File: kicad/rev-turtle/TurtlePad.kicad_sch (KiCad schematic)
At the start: 15 parts, among them SW1 SW_Push, U1 ProMicro

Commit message: rev1.1 again
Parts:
- removed MX8: MX-NoLED, 0xcb:SW_Cherry_MX_PCB_1.00u, symbol MX_Alps_Hybrid:MX-NoLED
- removed OL1: SSD1306, SSD1306:128x64OLED, symbol SSD1306-128x64_OLED:SSD1306
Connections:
- net GND: now also MX3.1 (COL), MX4.1 (COL), MX7.1 (COL); no longer MX3.2 (ROW), MX4.2 (ROW), MX7.2 (ROW)
- net MX3: now also MX3.2 (ROW); no longer MX3.1 (COL)
- net MX4: now also MX4.2 (ROW); no longer MX4.1 (COL)
- net MX7: now also MX7.2 (ROW); no longer MX7.1 (COL)
- net MX8: no longer names the net of U1.13 (10/PB6)
- net SCL: no longer names the net of U1.6 (3/PD0)
- net SDA: no longer names the net of U1.5 (2/PD1)
- no-connect marks 9 -> 12
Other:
- moved on the sheet: MX1, MX2, MX3, MX4, MX5, MX6, MX7

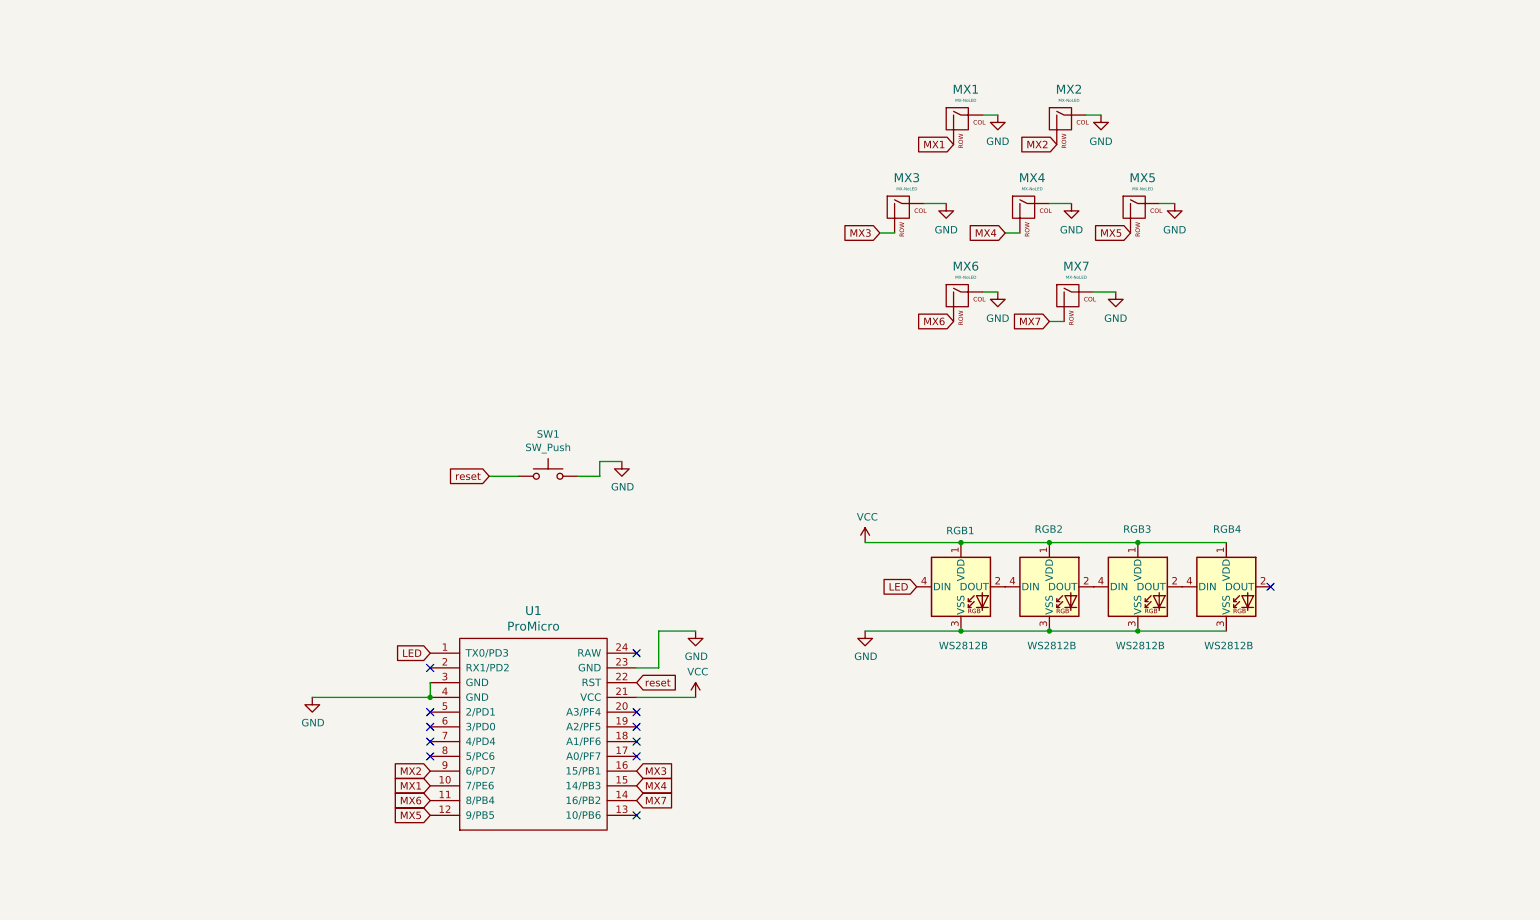
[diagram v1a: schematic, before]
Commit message: Redid schematic because I am an idiot
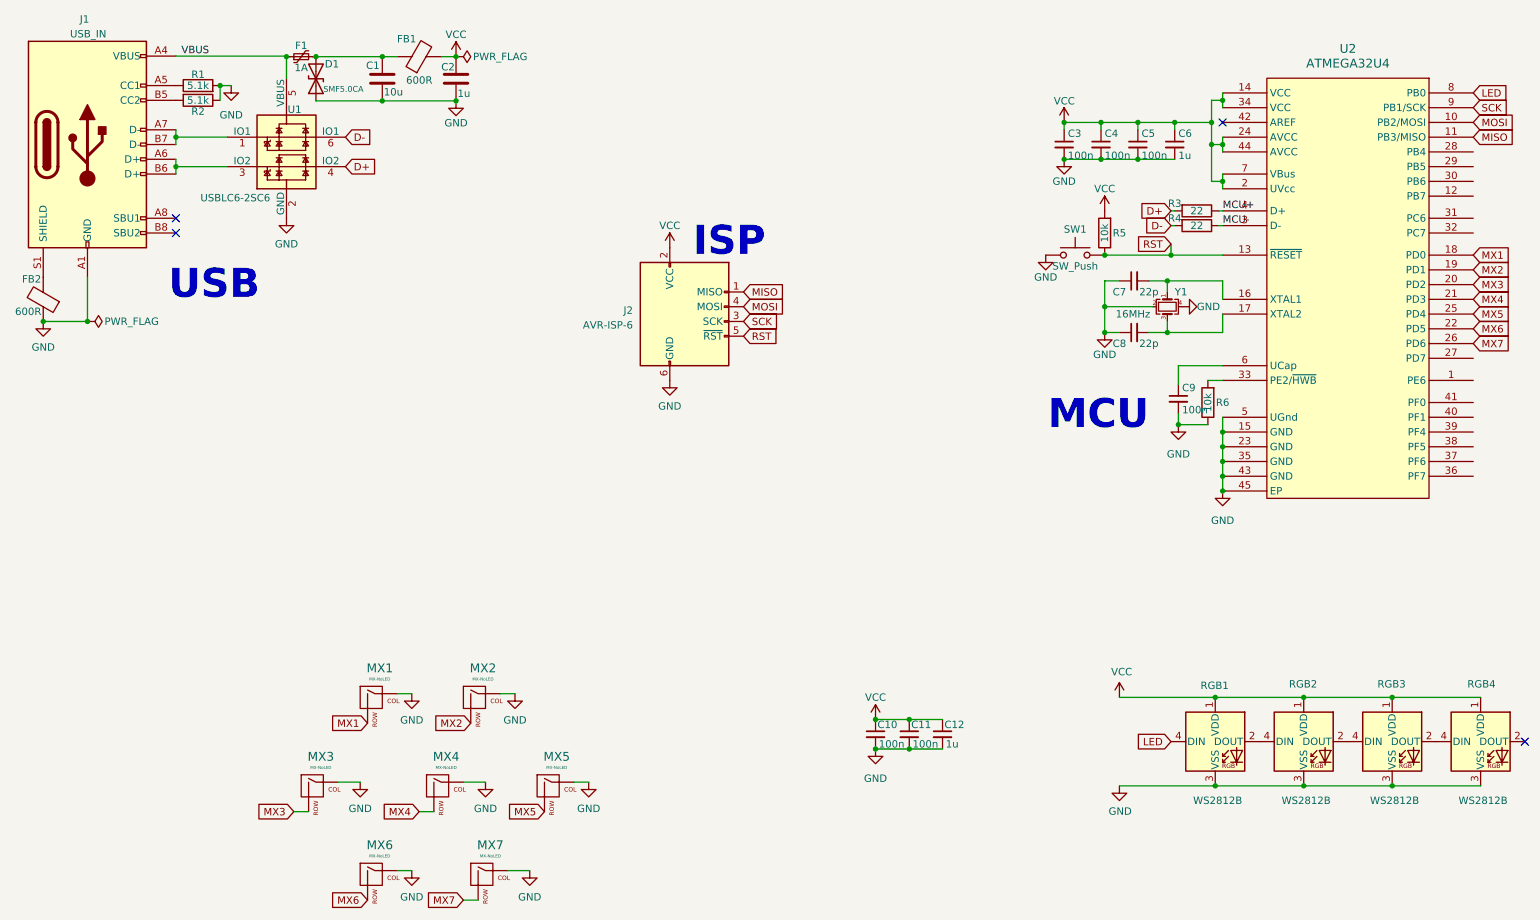
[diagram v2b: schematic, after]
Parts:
- removed U1: ProMicro, Keebio-Parts:ArduinoProMicro, symbol keebio:ProMicro
- added C1: 10u, Capacitor_SMD:C_0603_1608Metric, symbol Device:C
- added C10, C11, C3, C4, C5, C9: 100n, Capacitor_SMD:C_0603_1608Metric, symbol Device:C_Small
- added C12, C6: 1u, Capacitor_SMD:C_0603_1608Metric, symbol Device:C_Small
- added C2: 1u, Capacitor_SMD:C_0603_1608Metric, symbol Device:C
- added C7, C8: 22p, Capacitor_SMD:C_0603_1608Metric, symbol Device:C_Small
- added D1: SMF5.0CA, Diode_SMD:D_SOD-123F, symbol Device:D_TVS
- added F1: 1A, 0xcb:Fuse_0805_2012Metric, symbol Device:Polyfuse_Small
- added FB1: 600R, 0xcb:Ferrite_Bead_0603, symbol Device:FerriteBead
- added FB2: 600R, 0xcb:Ferrite_Bead_0603, symbol 0xcb:Ferrite_Bead
- added J1: USB_IN, 0xcb:molex2169900001, symbol Connector:USB_C_Receptacle_USB2.0
- added J2: AVR-ISP-6, 0xcb:AVR_PROG_2.54_THT, symbol Connector:AVR-ISP-6
- added R1, R2: 5.1k, Resistor_SMD:R_0603_1608Metric, symbol Device:R
- added R3, R4: 22, Resistor_SMD:R_0603_1608Metric, symbol Device:R
- added R5, R6: 10k, Resistor_SMD:R_0603_1608Metric, symbol Device:R
- added U1: USBLC6-2SC6, Package_TO_SOT_SMD:SOT-23-6, symbol 0xcb:USBLC6-2SC6
- added U2: ATMEGA32U4, 0xcb:QFN-44-1EP_7x7mm_P0.5mm_EP5.2x5.2mm_ThermalVias, symbol 0xcb:ATMEGA32U4
- added Y1: 16MHz, 0xcb:Crystal_SMD_3225-4Pin_3.2x2.5mm, symbol Device:Crystal_GND24_Small
- RGB1, RGB2, RGB3, RGB4: footprint Keebio-Parts:WS2812B -> LED_SMD:LED_WS2812B_PLCC4_5.0x5.0mm_P3.2mm
- SW1: footprint Keebio-Parts:SW_Tactile_SPST_Angled_MJTP1117 -> Button_Switch_SMD:SW_SPST_TL3342; Alt Part Nb. (none) -> C318884; Part Nb. (none) -> EG2531CT-ND
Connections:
- net reset is gone; now on net GND: SW1.1
- net GND: now also C1.2, C10.2, C11.2, C12.2, C2.2, C3.2, C4.2, C5.2, C6.2, C7.1, C8.1, C9.2, D1.1 (A1), FB2.1, J1.A1 (GND), J1.A12 (GND), J1.B1 (GND), J1.B12 (GND), J2.6 (GND), R1.2, R2.1, R6.1, U1.2 (GND), U2.15 (GND), U2.23 (GND), U2.35 (GND), U2.43 (GND), U2.45 (EP), U2.5 (UGnd), Y1.2, Y1.4; no longer SW1.2
- net LED: now also U2.8 (PB0)
- net MX1: now also U2.18 (PD0)
- net MX2: now also U2.19 (PD1)
- net MX3: now also U2.20 (PD2)
- net MX4: now also U2.21 (PD3)
- net MX5: now also U2.25 (PD4)
- net MX6: now also U2.22 (PD5)
- net MX7: now also U2.26 (PD6)
- net VCC: now also C10.1, C11.1, C12.1, C2.1, C3.1, C4.1, C5.1, C6.1, FB1.2, J2.2 (VCC), R5.2, U2.14 (VCC), U2.2 (UVcc), U2.24 (AVCC), U2.34 (VCC), U2.44 (AVCC), U2.7 (VBus)
- new net: J1.B5 (CC2), R2.2
- new net: FB2.2, J1.S1 (SHIELD)
- new net: C8.2, U2.17 (XTAL2), Y1.3
- new net: C7.2, U2.16 (XTAL1), Y1.1
- new net: C1.1, D1.2 (A2), F1.2, FB1.1
- new net: C9.1, U2.6 (UCap)
- new net: J1.A7 (D-), J1.B7 (D-), U1.1 (IO1)
- new net: J1.A6 (D+), J1.B6 (D+), U1.3 (IO2)
- new net: R6.2, U2.33 (PE2/~{HWB})
- new net: J1.A5 (CC1), R1.1
- new net D+: R3.2, U1.4 (IO2)
- new net D-: R4.2, U1.6 (IO1)
- new net MCU+: R3.1, U2.4 (D+)
- new net MCU-: R4.1, U2.3 (D-)
- new net MISO: J2.1 (MISO), U2.11 (PB3/MISO)
- new net MOSI: J2.4 (MOSI), U2.10 (PB2/MOSI)
- new net RST: J2.5 (~{RST}), R5.1, SW1.2, U2.13 (~{RESET})
- new net SCK: J2.3 (SCK), U2.9 (PB1/SCK)
- new net VBUS: F1.1, J1.A4 (VBUS), J1.A9 (VBUS), J1.B4 (VBUS), J1.B9 (VBUS), U1.5 (VBUS)
- no-connect marks 12 -> 4
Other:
- note added: "ISP"
- note added: "MCU"
- note added: "USB"
- moved on the sheet: MX1, MX2, MX3, MX4, MX5, MX6, MX7, RGB1, RGB2, RGB3, RGB4

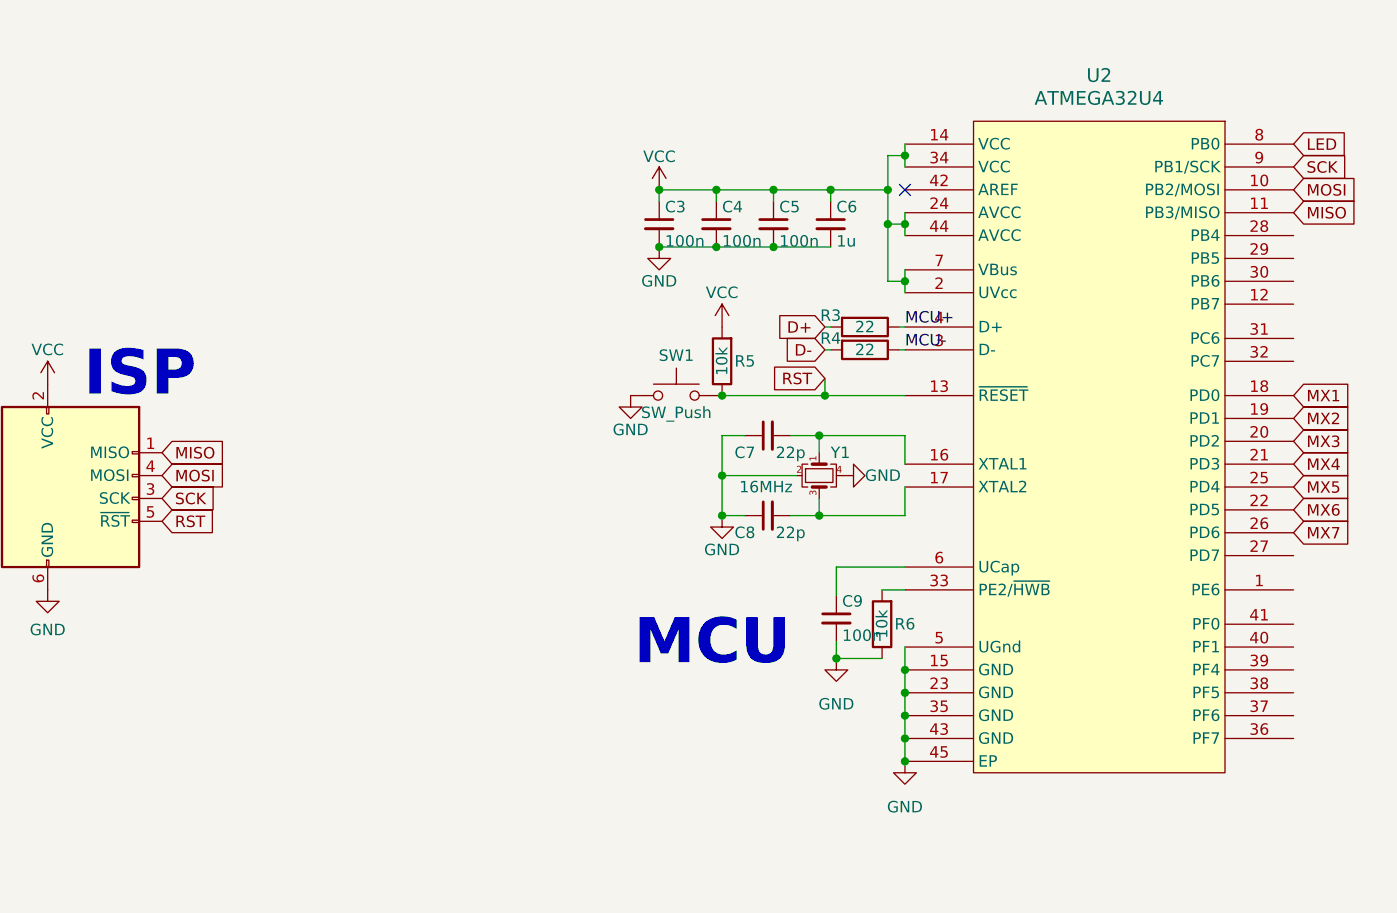
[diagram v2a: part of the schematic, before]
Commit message: Placed and routed all components on PCB
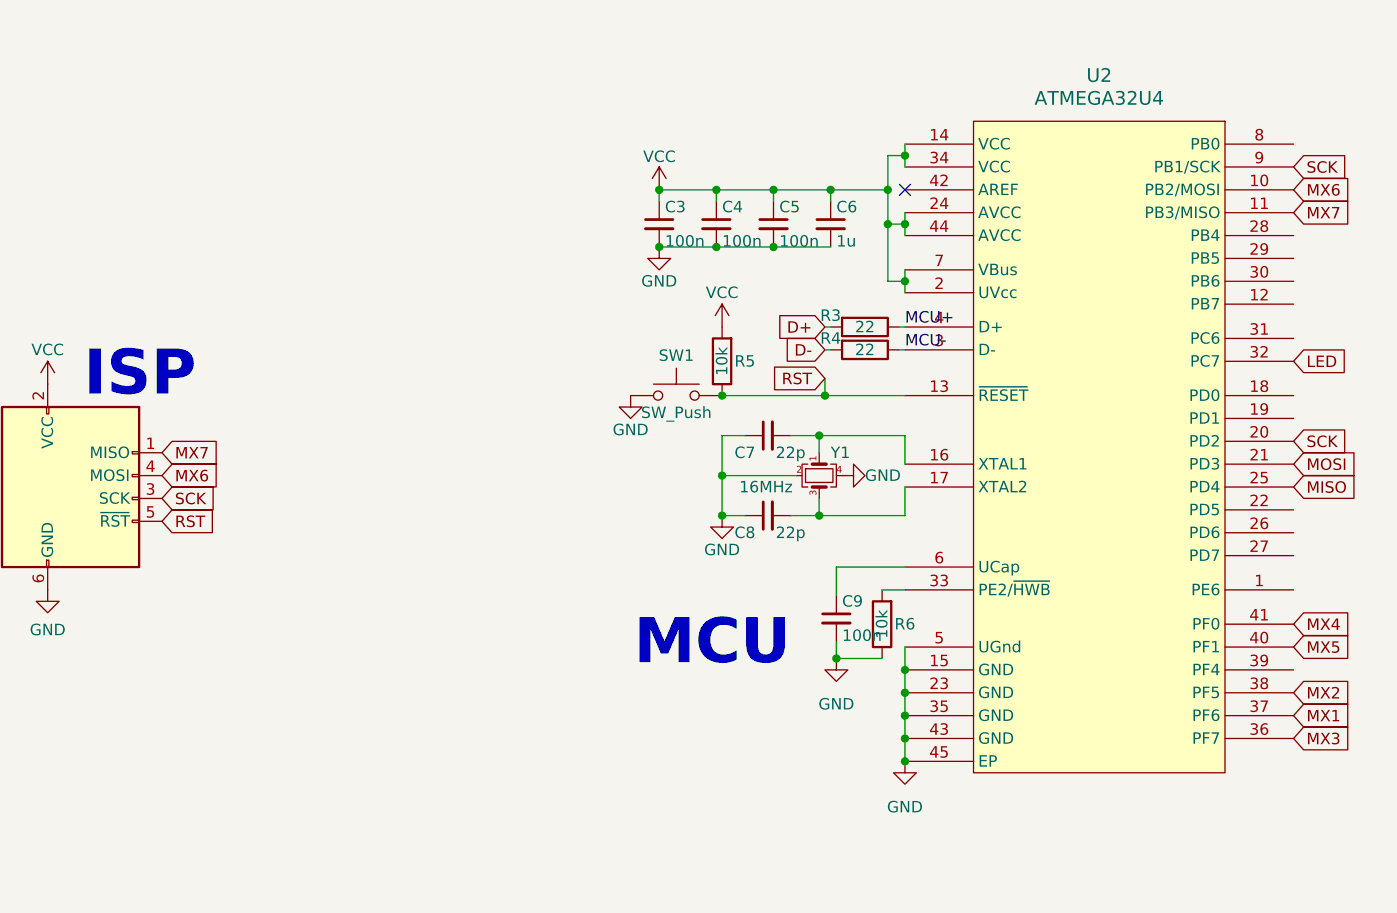
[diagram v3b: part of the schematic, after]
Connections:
- net LED: now also U2.32 (PC7); no longer U2.8 (PB0)
- net MISO: now also U2.25 (PD4); no longer J2.1 (MISO), U2.11 (PB3/MISO)
- net MOSI: now also U2.21 (PD3); no longer J2.4 (MOSI), U2.10 (PB2/MOSI)
- net MX1: now also U2.37 (PF6); no longer U2.18 (PD0)
- net MX2: now also U2.38 (PF5); no longer U2.19 (PD1)
- net MX3: now also U2.36 (PF7); no longer U2.20 (PD2)
- net MX4: now also U2.41 (PF0); no longer U2.21 (PD3)
- net MX5: now also U2.40 (PF1); no longer U2.25 (PD4)
- net MX6: now also J2.4 (MOSI), U2.10 (PB2/MOSI); no longer U2.22 (PD5)
- net MX7: now also J2.1 (MISO), U2.11 (PB3/MISO); no longer U2.26 (PD6)
- net SCK: now also U2.20 (PD2)
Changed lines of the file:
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@@
     (effects (font (size 1.27 1.27)) (justify left bottom))
   )
-  (global_label "MISO" (shape input) (at 139.065 60.96 0) (fields_autoplaced)
+  (global_label "MX7" (shape input) (at 139.065 60.96 0) (fields_autoplaced)
     (effects (font (size 1.27 1.27)) (justify left))
-    (property "Intersheet References" "${INTERSHEET_REFS}" (id 0) (at 146.2648 60.8806 0)
+    (property "Intersheet References" "${INTERSHEET_REFS}" (id 0) (at 145.2597 60.8806 0)
       (effects (font (size 1.27 1.27)) (justify left) hide)
     )
@@
     )
   )
-  (global_label "MOSI" (shape input) (at 139.065 63.5 0) (fields_autoplaced)
+  (global_label "MX6" (shape input) (at 139.065 63.5 0) (fields_autoplaced)
     (effects (font (size 1.27 1.27)) (justify left))
-    (property "Intersheet References" "${INTERSHEET_REFS}" (id 0) (at 146.2648 63.4206 0)
+    (property "Intersheet References" "${INTERSHEET_REFS}" (id 0) (at 145.2597 63.4206 0)
       (effects (font (size 1.27 1.27)) (justify left) hide)
     )
@@
     )
   )
-  (global_label "MX6" (shape input) (at 264.795 67.31 0) (fields_autoplaced)
+  (global_label "MX6" (shape input) (at 264.795 31.75 0) (fields_autoplaced)
     (effects (font (size 1.27 1.27)) (justify left))
-    (property "Intersheet References" "${INTERSHEET_REFS}" (id 0) (at 270.9897 67.2306 0)
+    (property "Intersheet References" "${INTERSHEET_REFS}" (id 0) (at 270.9897 31.6706 0)
       (effects (font (size 1.27 1.27)) (justify left) hide)
     )
@@
     )
   )
+  (global_label "SCK" (shape input) (at 264.795 29.21 0) (fields_autoplaced)
+    (effects (font (size 1.27 1.27)) (justify left))
+    (property "Intersheet References" "${INTERSHEET_REFS}" (id 0) (at 270.8687 29.1306 0)
+      (effects (font (size 1.27 1.27)) (justify left) hide)
+    )
+  )
   (global_label "D+" (shape input) (at 212.725 46.99 180) (fields_autoplaced)
     (effects (font (size 1.27 1.27)) (justify right))
@@
     )
   )
-  (global_label "MX3" (shape input) (at 264.795 59.69 0) (fields_autoplaced)
+  (global_label "MX3" (shape input) (at 264.795 92.71 0) (fields_autoplaced)
     (effects (font (size 1.27 1.27)) (justify left))
-    (property "Intersheet References" "${INTERSHEET_REFS}" (id 0) (at 270.9897 59.6106 0)
+    (property "Intersheet References" "${INTERSHEET_REFS}" (id 0) (at 270.9897 92.6306 0)
       (effects (font (size 1.27 1.27)) (justify left) hide)
     )
   )
-  (global_label "MX2" (shape input) (at 264.795 57.15 0) (fields_autoplaced)
+  (global_label "MX2" (shape input) (at 264.795 87.63 0) (fields_autoplaced)
     (effects (font (size 1.27 1.27)) (justify left))
-    (property "Intersheet References" "${INTERSHEET_REFS}" (id 0) (at 270.9897 57.0706 0)
+    (property "Intersheet References" "${INTERSHEET_REFS}" (id 0) (at 270.9897 87.5506 0)
       (effects (font (size 1.27 1.27)) (justify left) hide)
     )
@@
     )
   )
-  (global_label "LED" (shape input) (at 264.795 26.67 0) (fields_autoplaced)
+  (global_label "LED" (shape input) (at 264.795 50.8 0) (fields_autoplaced)
     (effects (font (size 1.27 1.27)) (justify left))
-    (property "Intersheet References" "${INTERSHEET_REFS}" (id 0) (at 270.5663 26.5906 0)
+    (property "Intersheet References" "${INTERSHEET_REFS}" (id 0) (at 270.5663 50.7206 0)
       (effects (font (size 1.27 1.27)) (justify left) hide)
     )
   )
-  (global_label "MISO" (shape input) (at 264.795 34.29 0) (fields_autoplaced)
+  (global_label "MISO" (shape input) (at 264.795 64.77 0) (fields_autoplaced)
     (effects (font (size 1.27 1.27)) (justify left))
-    (property "Intersheet References" "${INTERSHEET_REFS}" (id 0) (at 271.9948 34.2106 0)
+    (property "Intersheet References" "${INTERSHEET_REFS}" (id 0) (at 271.9948 64.6906 0)
       (effects (font (size 1.27 1.27)) (justify left) hide)
     )
   )
-  (global_label "MX4" (shape input) (at 264.795 62.23 0) (fields_autoplaced)
+  (global_label "MX4" (shape input) (at 264.795 80.01 0) (fields_autoplaced)
     (effects (font (size 1.27 1.27)) (justify left))
-    (property "Intersheet References" "${INTERSHEET_REFS}" (id 0) (at 270.9897 62.1506 0)
+    (property "Intersheet References" "${INTERSHEET_REFS}" (id 0) (at 270.9897 79.9306 0)
       (effects (font (size 1.27 1.27)) (justify left) hide)
     )
   )
-  (global_label "MX5" (shape input) (at 264.795 64.77 0) (fields_autoplaced)
+  (global_label "MX5" (shape input) (at 264.795 82.55 0) (fields_autoplaced)
     (effects (font (size 1.27 1.27)) (justify left))
-    (property "Intersheet References" "${INTERSHEET_REFS}" (id 0) (at 270.9897 64.6906 0)
+    (property "Intersheet References" "${INTERSHEET_REFS}" (id 0) (at 270.9897 82.4706 0)
       (effects (font (size 1.27 1.27)) (justify left) hide)
     )
@@
     )
   )
-  (global_label "MOSI" (shape input) (at 264.795 31.75 0) (fields_autoplaced)
+  (global_label "MOSI" (shape input) (at 264.795 62.23 0) (fields_autoplaced)
     (effects (font (size 1.27 1.27)) (justify left))
-    (property "Intersheet References" "${INTERSHEET_REFS}" (id 0) (at 271.9948 31.6706 0)
+    (property "Intersheet References" "${INTERSHEET_REFS}" (id 0) (at 271.9948 62.1506 0)
       (effects (font (size 1.27 1.27)) (justify left) hide)
     )
   )
-  (global_label "MX1" (shape input) (at 264.795 54.61 0) (fields_autoplaced)
+  (global_label "MX1" (shape input) (at 264.795 90.17 0) (fields_autoplaced)
     (effects (font (size 1.27 1.27)) (justify left))
-    (property "Intersheet References" "${INTERSHEET_REFS}" (id 0) (at 270.9897 54.5306 0)
+    (property "Intersheet References" "${INTERSHEET_REFS}" (id 0) (at 270.9897 90.0906 0)
       (effects (font (size 1.27 1.27)) (justify left) hide)
     )
   )
-  (global_label "SCK" (shape input) (at 264.795 29.21 0) (fields_autoplaced)
+  (global_label "SCK" (shape input) (at 264.795 59.69 0) (fields_autoplaced)
     (effects (font (size 1.27 1.27)) (justify left))
-    (property "Intersheet References" "${INTERSHEET_REFS}" (id 0) (at 270.8687 29.1306 0)
+    (property "Intersheet References" "${INTERSHEET_REFS}" (id 0) (at 270.8687 59.6106 0)
       (effects (font (size 1.27 1.27)) (justify left) hide)
     )
@@
     )
   )
-  (global_label "MX7" (shape input) (at 264.795 69.85 0) (fields_autoplaced)
+  (global_label "MX7" (shape input) (at 264.795 34.29 0) (fields_autoplaced)
     (effects (font (size 1.27 1.27)) (justify left))
-    (property "Intersheet References" "${INTERSHEET_REFS}" (id 0) (at 270.9897 69.7706 0)
+    (property "Intersheet References" "${INTERSHEET_REFS}" (id 0) (at 270.9897 34.2106 0)
       (effects (font (size 1.27 1.27)) (justify left) hide)
     )
